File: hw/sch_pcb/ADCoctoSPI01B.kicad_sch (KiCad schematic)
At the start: 80 parts, among them J1 SATA7-67491-1030, J10 SAS_mini_1888174, J11 +5V, J2 SATA7-67491-1030, J3 SATA7-67491-1030, J4 SATA7-67491-1030, J5 HEADER_1x02, J6 HEADER_1x02, J7 SATA7-67491-1030, J8 HEADER_2x04, J9 HEADER_1x02, M1 HOLE, M2 HOLE, M3 HOLE, M4 HOLE, U1 AFE5801, U2 LM1117MP-1,8/NO, U3 LM1117MP-3,3/NO

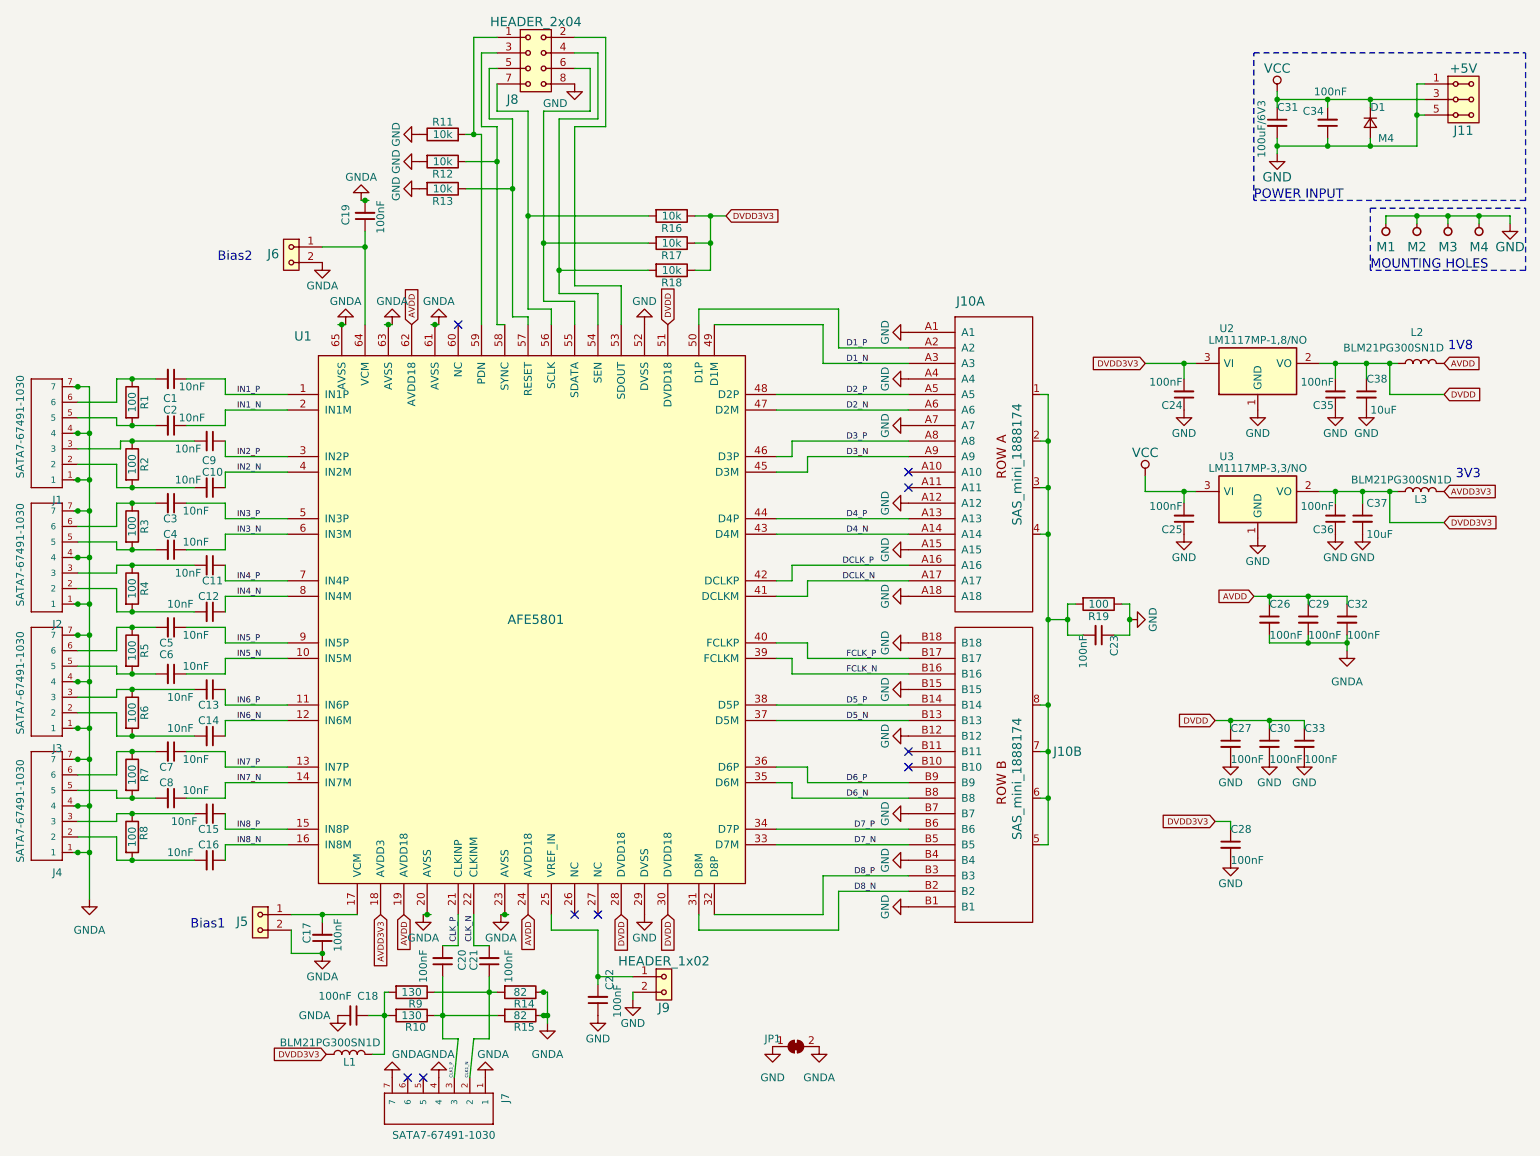
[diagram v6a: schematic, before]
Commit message: doroutovani cest
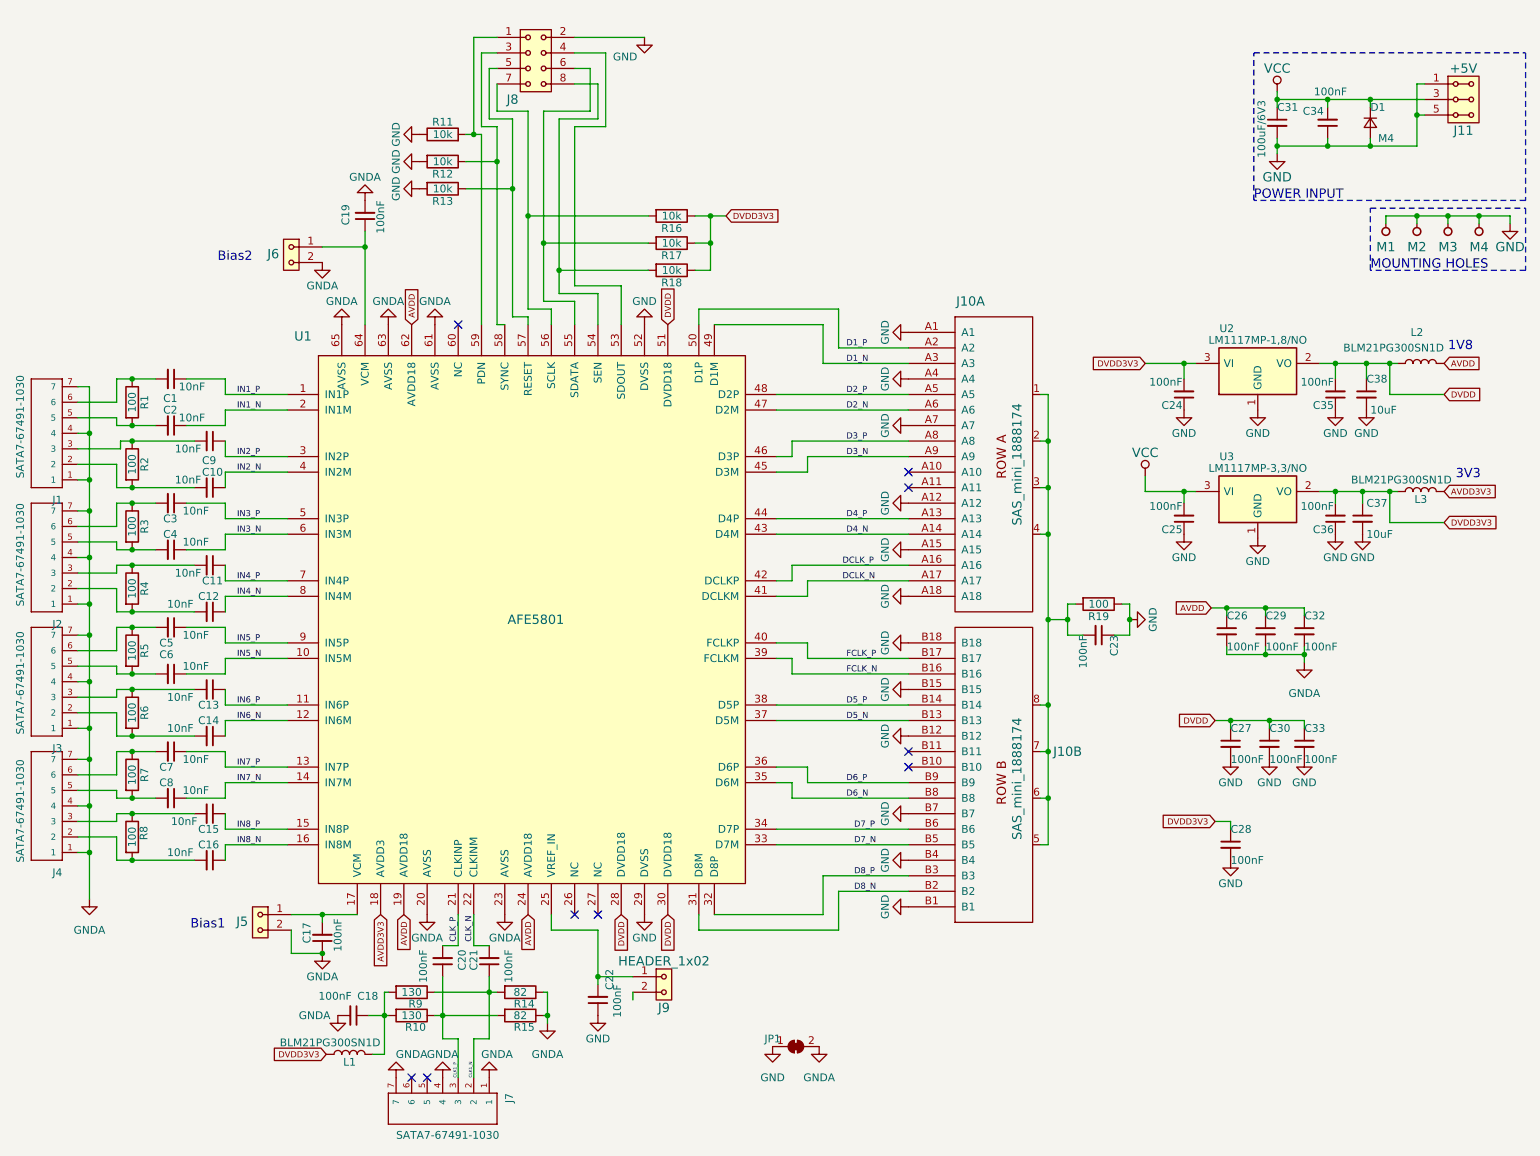
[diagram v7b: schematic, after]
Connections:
- net GND: now also J8.2; no longer J8.8, J9.2
- net at U1.53 (SDOUT): now also J8.4; no longer J8.2
- net at R18.2, U1.54 (SEN): now also J8.8; no longer J8.4
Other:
- moved on the sheet: C26, C29, C32, J7

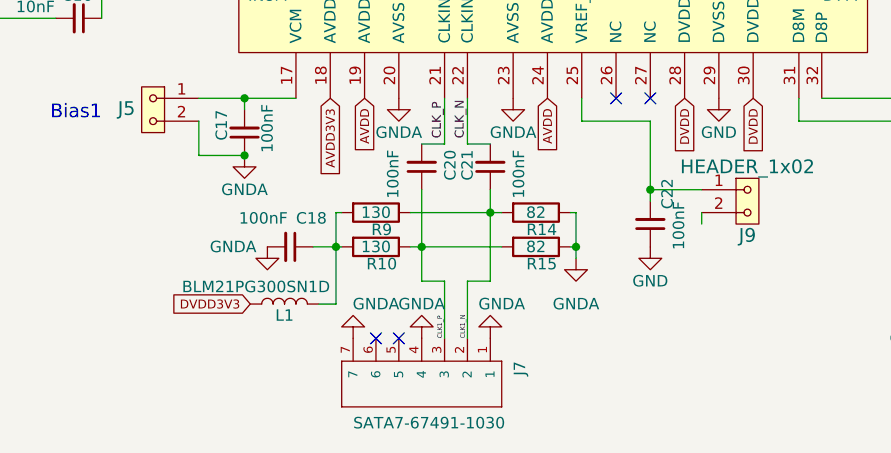
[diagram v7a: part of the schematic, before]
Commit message: uprava routovani, premisteni soucastek, AVDD k hodinam
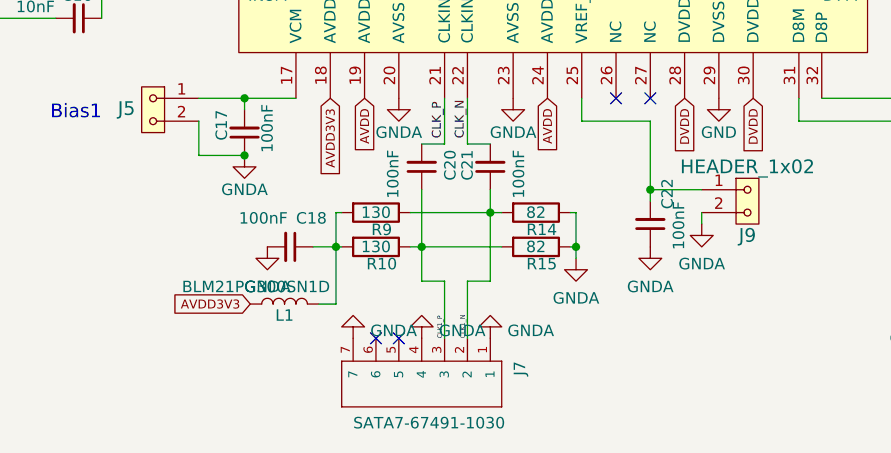
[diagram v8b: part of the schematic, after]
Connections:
- net AVDD3V3: now also L1.1
- net DVDD3V3: no longer L1.1
- net GND: no longer C22.1
- net GNDA: now also C22.1, J9.2
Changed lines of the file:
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@@
-    )
-  )
-  (global_label "DVDD3V3" (shape input) (at 81.915 182.88 180) (fields_autoplaced)
-    (effects (font (size 0.9906 0.9906)) (justify right))
-    (property "Intersheet References" "${INTERSHEET_REFS}" (id 0) (at 0 0 0)
-      (effects (font (size 1.27 1.27)) hide)
     )
   )
@@
     (effects (font (size 0.9906 0.9906)) (justify right))
     (property "Intersheet References" "${INTERSHEET_REFS}" (id 0) (at 0 0 0)
+      (effects (font (size 1.27 1.27)) hide)
+    )
+  )
+  (global_label "AVDD3V3" (shape input) (at 81.915 182.88 180) (fields_autoplaced)
+    (effects (font (size 0.9906 0.9906)) (justify right))
+    (property "Intersheet References" "${INTERSHEET_REFS}" (id 0) (at 241.935 92.075 0)
       (effects (font (size 1.27 1.27)) hide)
     )
@@
     (pin "2")
   )
-  (symbol (lib_id "ADCoctoSPI01A-rescue:GND-power") (at 126.365 176.53 0) (unit 1)
-    (in_bom yes) (on_board yes)
-    (property "Reference" "#PWR032" (id 0) (at 126.365 182.88 0)
-      (effects (font (size 1.27 1.27)) hide)
-    )
-    (property "Value" "GND" (id 1) (at 126.365 180.34 0))
-    (property "Footprint" "" (id 2) (at 126.365 176.53 0)
-      (effects (font (size 1.27 1.27)) hide)
-    )
-    (property "Datasheet" "" (id 3) (at 126.365 176.53 0)
-      (effects (font (size 1.27 1.27)) hide)
-    )
-    (pin "1")
-  )
   (symbol (lib_id "ADCoctoSPI01A-rescue:HEADER_1x02-MLAB_HEADER") (at 137.16 171.45 0) (unit 1)
     (in_bom yes) (on_board yes)
@@
     (pin "1")
   )
+  (symbol (lib_id "power:GNDA") (at 118.11 177.8 0) (unit 1)
+    (in_bom yes) (on_board yes) (fields_autoplaced)
+    (property "Reference" "#PWR0107" (id 0) (at 118.11 184.15 0)
+      (effects (font (size 1.27 1.27)) hide)
+    )
+    (property "Value" "GNDA" (id 1) (at 118.11 182.2434 0))
+    (property "Footprint" "" (id 2) (at 118.11 177.8 0)
+      (effects (font (size 1.27 1.27)) hide)
+    )
+    (property "Datasheet" "" (id 3) (at 118.11 177.8 0)
+      (effects (font (size 1.27 1.27)) hide)
+    )
+    (pin "1")
+  )
+  (symbol (lib_id "power:GNDA") (at 83.82 176.53 0) (unit 1)
+    (in_bom yes) (on_board yes) (fields_autoplaced)
+    (property "Reference" "#PWR0103" (id 0) (at 83.82 182.88 0)
+      (effects (font (size 1.27 1.27)) hide)
+    )
+    (property "Value" "GNDA" (id 1) (at 83.82 180.9734 0))
+    (property "Footprint" "" (id 2) (at 83.82 176.53 0)
+      (effects (font (size 1.27 1.27)) hide)
+    )
+    (property "Datasheet" "" (id 3) (at 83.82 176.53 0)
+      (effects (font (size 1.27 1.27)) hide)
+    )
+    (pin "1")
+  )
   (symbol (lib_id "power:GNDA") (at 81.28 166.37 0) (unit 1)
     (in_bom yes) (on_board yes)
@@
     (pin "1")
   )
-  (symbol (lib_id "power:GNDA") (at 93.345 186.69 180) (unit 1)
-    (in_bom yes) (on_board yes)
-    (property "Reference" "#PWR0104" (id 0) (at 93.345 180.34 0)
-      (effects (font (size 1.27 1.27)) hide)
-    )
-    (property "Value" "GNDA" (id 1) (at 95.885 182.88 0))
-    (property "Footprint" "" (id 2) (at 93.345 186.69 0)
-      (effects (font (size 1.27 1.27)) hide)
-    )
-    (property "Datasheet" "" (id 3) (at 93.345 186.69 0)
+  (symbol (lib_id "power:GNDA") (at 100.965 186.69 180) (unit 1)
+    (in_bom yes) (on_board yes) (fields_autoplaced)
+    (property "Reference" "#PWR0105" (id 0) (at 100.965 180.34 0)
+      (effects (font (size 1.27 1.27)) hide)
+    )
+    (property "Value" "GNDA" (id 1) (at 102.87 185.8538 0)
+      (effects (font (size 1.27 1.27)) (justify right))
+    )
+    (property "Footprint" "" (id 2) (at 100.965 186.69 0)
+      (effects (font (size 1.27 1.27)) hide)
+    )
+    (property "Datasheet" "" (id 3) (at 100.965 186.69 0)
       (effects (font (size 1.27 1.27)) hide)
     )
@@
     (pin "1")
   )
-  (symbol (lib_id "power:GNDA") (at 108.585 186.69 180) (unit 1)
-    (in_bom yes) (on_board yes)
-    (property "Reference" "#PWR0106" (id 0) (at 108.585 180.34 0)
-      (effects (font (size 1.27 1.27)) hide)
-    )
-    (property "Value" "GNDA" (id 1) (at 109.855 182.88 0))
-    (property "Footprint" "" (id 2) (at 108.585 186.69 0)
-      (effects (font (size 1.27 1.27)) hide)
-    )
-    (property "Datasheet" "" (id 3) (at 108.585 186.69 0)
-      (effects (font (size 1.27 1.27)) hide)
-    )
-    (pin "1")
-  )
-  (symbol (lib_id "power:GNDA") (at 83.82 176.53 0) (unit 1)
-    (in_bom yes) (on_board yes)
-    (property "Reference" "#PWR0103" (id 0) (at 83.82 182.88 0)
-      (effects (font (size 1.27 1.27)) hide)
-    )
-    (property "Value" "GNDA" (id 1) (at 80.01 176.53 0))
-    (property "Footprint" "" (id 2) (at 83.82 176.53 0)
-      (effects (font (size 1.27 1.27)) hide)
-    )
-    (property "Datasheet" "" (id 3) (at 83.82 176.53 0)
+  (symbol (lib_id "power:GNDA") (at 132.08 173.99 0) (unit 1)
+    (in_bom yes) (on_board yes) (fields_autoplaced)
+    (property "Reference" "#PWR0112" (id 0) (at 132.08 180.34 0)
+      (effects (font (size 1.27 1.27)) hide)
+    )
+    (property "Value" "GNDA" (id 1) (at 132.08 178.4334 0))
+    (property "Footprint" "" (id 2) (at 132.08 173.99 0)
+      (effects (font (size 1.27 1.27)) hide)
+    )
+    (property "Datasheet" "" (id 3) (at 132.08 173.99 0)
+      (effects (font (size 1.27 1.27)) hide)
+    )
+    (pin "1")
+  )
+  (symbol (lib_id "power:GNDA") (at 93.345 186.69 180) (unit 1)
+    (in_bom yes) (on_board yes) (fields_autoplaced)
+    (property "Reference" "#PWR0104" (id 0) (at 93.345 180.34 0)
+      (effects (font (size 1.27 1.27)) hide)
+    )
+    (property "Value" "GNDA" (id 1) (at 95.25 185.8538 0)
+      (effects (font (size 1.27 1.27)) (justify right))
+    )
+    (property "Footprint" "" (id 2) (at 93.345 186.69 0)
+      (effects (font (size 1.27 1.27)) hide)
+    )
+    (property "Datasheet" "" (id 3) (at 93.345 186.69 0)
       (effects (font (size 1.27 1.27)) hide)
     )
@@
     (pin "1")
   )
-  (symbol (lib_id "power:GNDA") (at 100.965 186.69 180) (unit 1)
-    (in_bom yes) (on_board yes)
-    (property "Reference" "#PWR0105" (id 0) (at 100.965 180.34 0)
-      (effects (font (size 1.27 1.27)) hide)
-    )
-    (property "Value" "GNDA" (id 1) (at 100.965 182.88 0))
-    (property "Footprint" "" (id 2) (at 100.965 186.69 0)
-      (effects (font (size 1.27 1.27)) hide)
-    )
-    (property "Datasheet" "" (id 3) (at 100.965 186.69 0)
-      (effects (font (size 1.27 1.27)) hide)
-    )
-    (pin "1")
-  )
-  (symbol (lib_id "power:GNDA") (at 118.11 177.8 0) (unit 1)
+  (symbol (lib_id "power:GNDA") (at 126.365 176.53 0) (unit 1)
     (in_bom yes) (on_board yes) (fields_autoplaced)
-    (property "Reference" "#PWR0107" (id 0) (at 118.11 184.15 0)
-      (effects (font (size 1.27 1.27)) hide)
-    )
-    (property "Value" "GNDA" (id 1) (at 118.11 182.88 0))
-    (property "Footprint" "" (id 2) (at 118.11 177.8 0)
-      (effects (font (size 1.27 1.27)) hide)
-    )
-    (property "Datasheet" "" (id 3) (at 118.11 177.8 0)
+    (property "Reference" "#PWR0111" (id 0) (at 126.365 182.88 0)
+      (effects (font (size 1.27 1.27)) hide)
+    )
+    (property "Value" "GNDA" (id 1) (at 126.365 180.9734 0))
+    (property "Footprint" "" (id 2) (at 126.365 176.53 0)
+      (effects (font (size 1.27 1.27)) hide)
+    )
+    (property "Datasheet" "" (id 3) (at 126.365 176.53 0)
+      (effects (font (size 1.27 1.27)) hide)
+    )
+    (pin "1")
+  )
+  (symbol (lib_id "power:GNDA") (at 108.585 186.69 180) (unit 1)
+    (in_bom yes) (on_board yes) (fields_autoplaced)
+    (property "Reference" "#PWR0106" (id 0) (at 108.585 180.34 0)
+      (effects (font (size 1.27 1.27)) hide)
+    )
+    (property "Value" "GNDA" (id 1) (at 110.49 185.8538 0)
+      (effects (font (size 1.27 1.27)) (justify right))
+    )
+    (property "Footprint" "" (id 2) (at 108.585 186.69 0)
+      (effects (font (size 1.27 1.27)) hide)
+    )
+    (property "Datasheet" "" (id 3) (at 108.585 186.69 0)
       (effects (font (size 1.27 1.27)) hide)
     )
@@
       (reference "#PWR031") (unit 1) (value "GND") (footprint "")
     )
-    (path "/00000000-0000-0000-0000-000059d79065"
-      (reference "#PWR032") (unit 1) (value "GND") (footprint "")
-    )
     (path "/00000000-0000-0000-0000-0000599de515"
       (reference "#PWR034") (unit 1) (value "GND") (footprint "")
@@
       (reference "#PWR0102") (unit 1) (value "GNDA") (footprint "")
     )
-    (path "/db4353a7-258c-4f66-b624-280533e6bcf2"
+    (path "/6c7f4967-11b7-4190-a43f-2b4472edbac1"
       (reference "#PWR0103") (unit 1) (value "GNDA") (footprint "")
     )
-    (path "/7326d5d8-6680-4437-8840-9e975f639d91"
+    (path "/e0d5d540-7a1e-4710-b537-297257a10229"
       (reference "#PWR0104") (unit 1) (value "GNDA") (footprint "")
     )
-    (path "/e6425b1d-052f-446a-abc6-8a9475735825"
+    (path "/7488c6d3-1997-420a-8dc9-9d1ceec554b1"
       (reference "#PWR0105") (unit 1) (value "GNDA") (footprint "")
     )
-    (path "/d269e413-7d16-452f-8821-523de3f0da24"
+    (path "/f825b398-b599-4327-a2e2-31dc03e6fff9"
       (reference "#PWR0106") (unit 1) (value "GNDA") (footprint "")
     )
-    (path "/f17a9bf7-e46e-41d0-9469-07c88bd27f50"
+    (path "/5bf6a21f-5895-4953-92b1-da84b53091ce"
       (reference "#PWR0107") (unit 1) (value "GNDA") (footprint "")
     )
@@
       (reference "#PWR0110") (unit 1) (value "GNDA") (footprint "")
     )
+    (path "/f68003c6-8b20-42cd-8655-75197ef68f36"
+      (reference "#PWR0111") (unit 1) (value "GNDA") (footprint "")
+    )
+    (path "/d742ad90-f22f-4a8c-882c-ea4fb226f14c"
+      (reference "#PWR0112") (unit 1) (value "GNDA") (footprint "")
+    )
     (path "/00000000-0000-0000-0000-00005999d4a4"
